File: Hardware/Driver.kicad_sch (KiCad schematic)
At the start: 16 parts, among them J301 Conn_01x06, J302 Conn_01x06, U301 ZXBM5210-SP, U303 ZXBM5210-SP

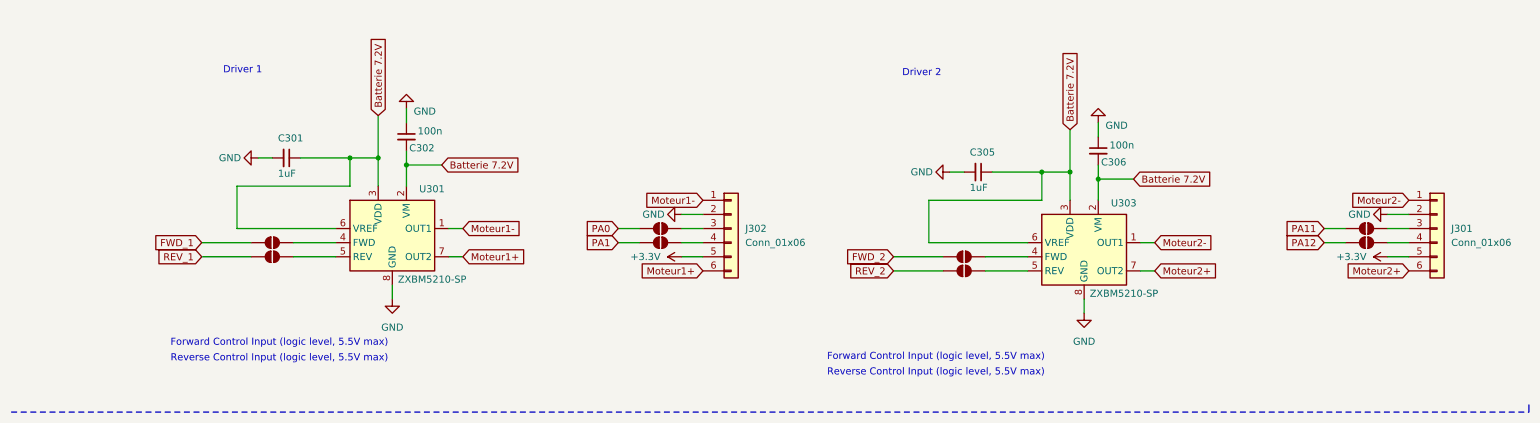
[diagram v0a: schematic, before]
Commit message: PCB - Updated Driver schematic
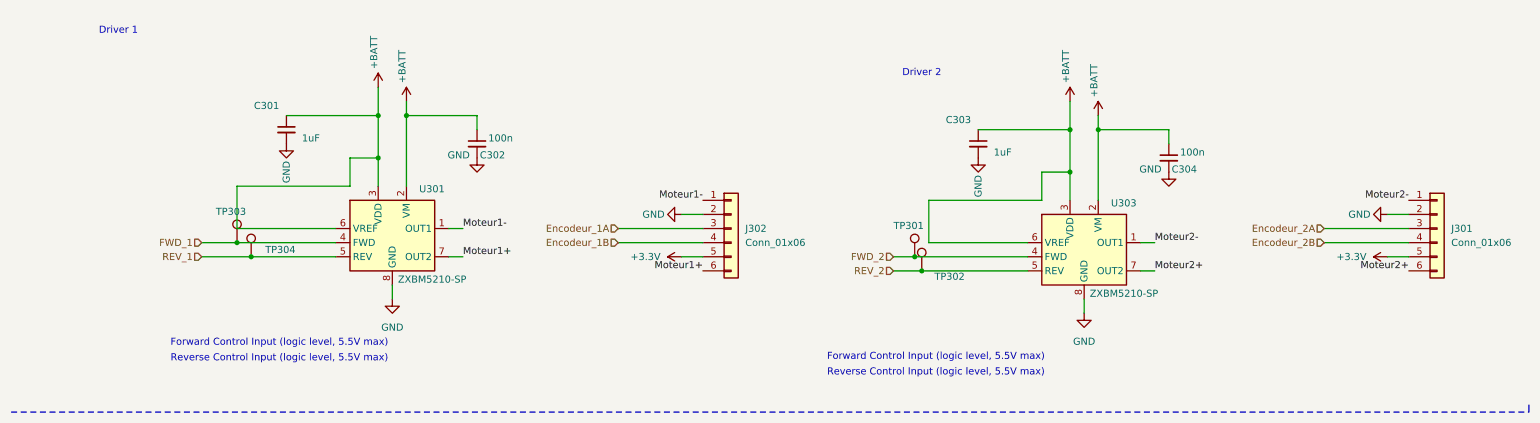
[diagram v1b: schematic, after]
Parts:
- removed C305: 1uF, Capacitor_SMD:C_0603_1608Metric, symbol Device:C_Small
- removed C306: 100n, Capacitor_SMD:C_0603_1608Metric, symbol Device:C_Small
- removed JP303, JP304, JP305, JP306, JP307, JP308, JP309, JP310: ~, symbol Jumper:SolderJumper_2_Open
- added C303: 1uF, Capacitor_SMD:C_0603_1608Metric, symbol Device:C_Small
- added C304: 100n, Capacitor_SMD:C_0603_1608Metric, symbol Device:C_Small
- added TP301, TP302, TP303, TP304: TestPoint, TestPoint:TestPoint_Pad_D1.5mm, symbol Connector:TestPoint
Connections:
- net FWD_1: now also U301.4 (FWD), TP303.1
- net FWD_2: now also U303.4 (FWD), TP301.1
- net GND: now also C302.2, C303.2, C304.2; no longer C302.1
- net REV_1: now also U301.5 (REV), TP304.1
- net REV_2: now also U303.5 (REV), TP302.1
- net Encodeur_1A: now reaches J302.3 (Pin_3)
- net Encodeur_1B: now reaches J302.4 (Pin_4)
- net Encodeur_2B: now reaches J301.4 (Pin_4)
- net Encodeur_2A: now reaches J301.3 (Pin_3)
- net Batterie 7.2V renamed +BATT
- net +BATT: now also C302.1, C303.1, C304.1; no longer C302.2
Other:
- moved on the sheet: C301, C302
